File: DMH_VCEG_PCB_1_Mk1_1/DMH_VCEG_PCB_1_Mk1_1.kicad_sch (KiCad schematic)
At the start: 0 parts

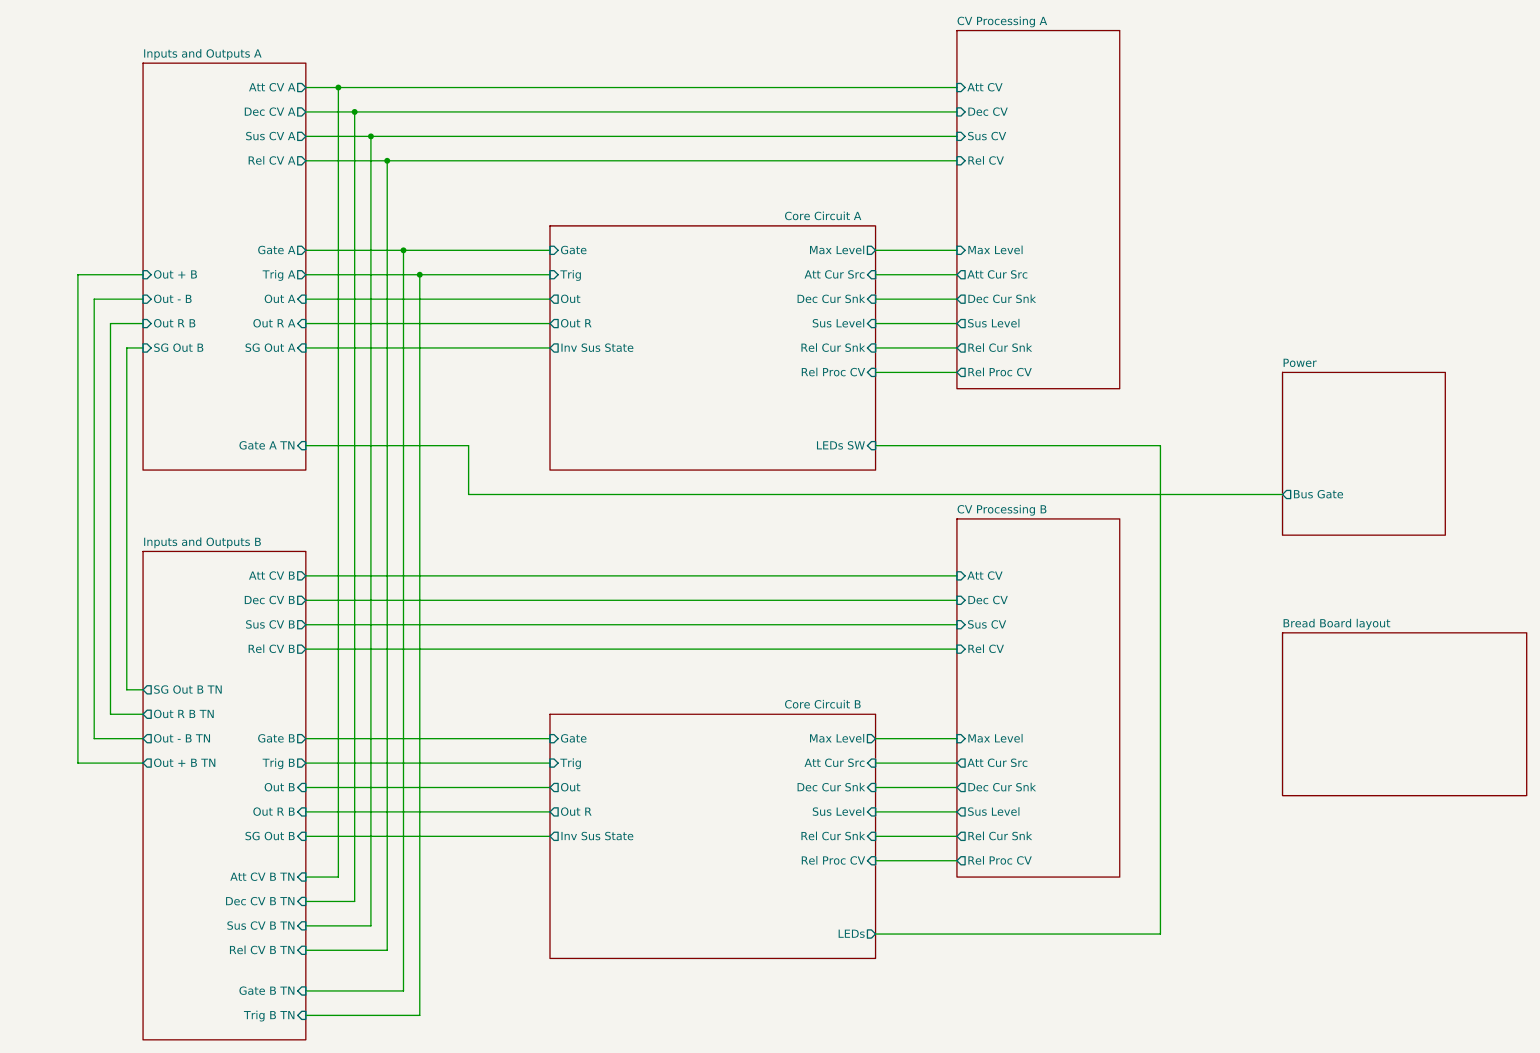
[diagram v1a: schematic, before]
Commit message: Fixed normalled tip routing for CV and Gate
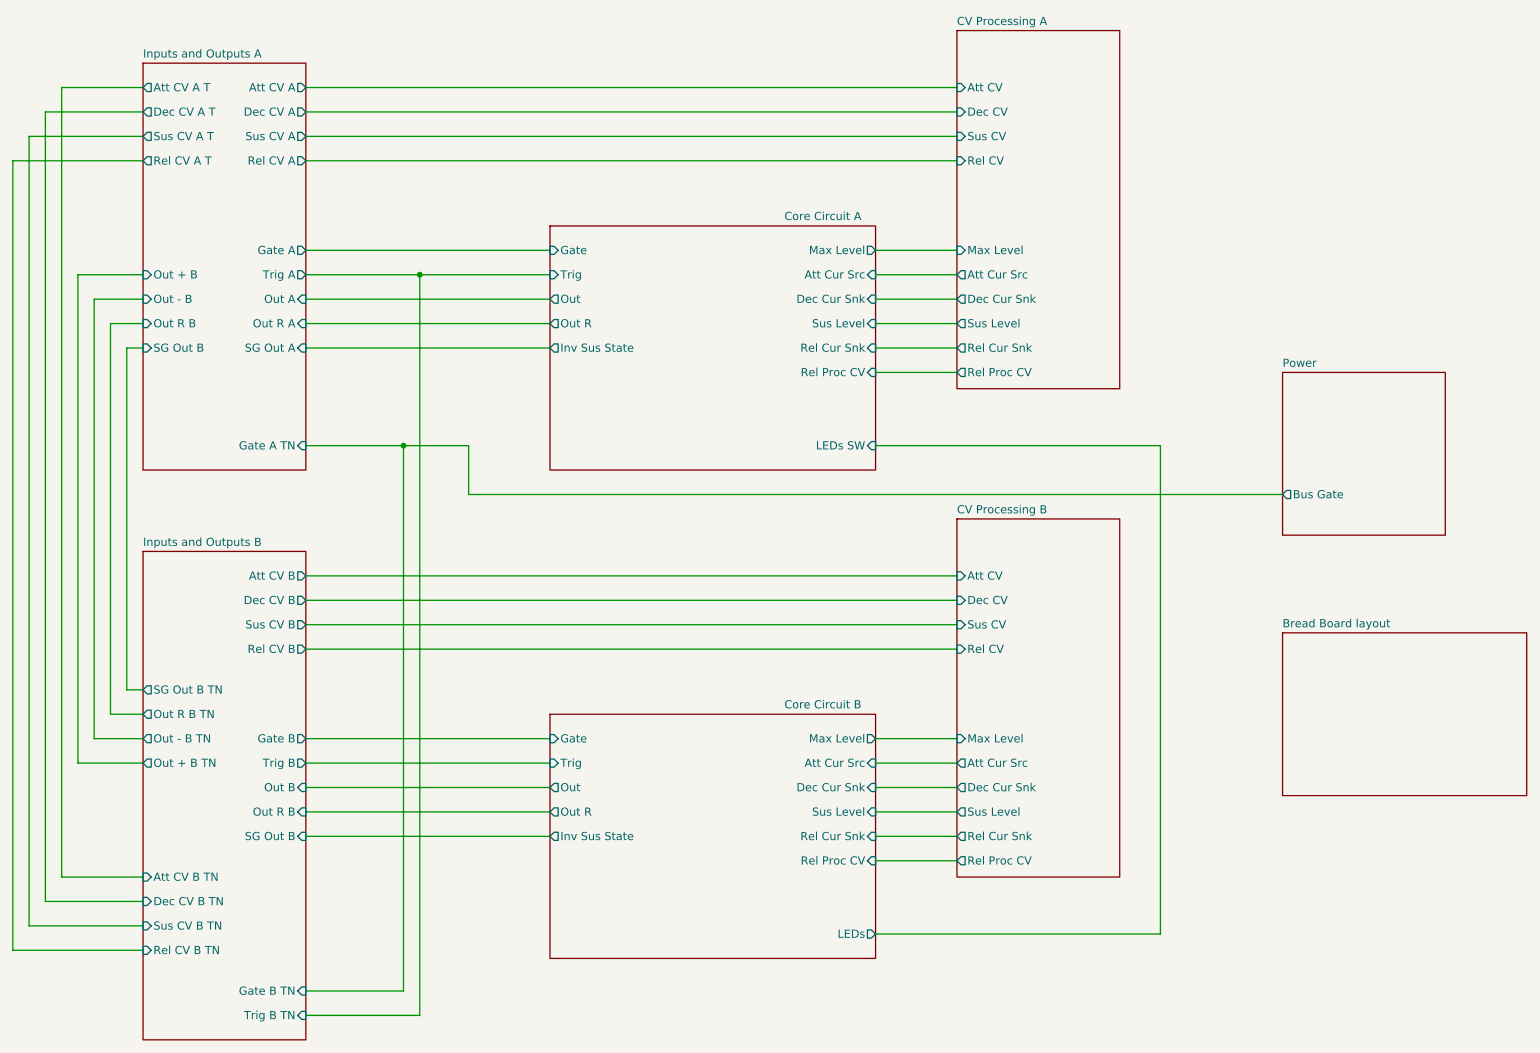
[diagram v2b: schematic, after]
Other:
- sheet Inputs and Outputs A ports: added Att CV A T, Dec CV A T, Rel CV A T, Sus CV A T; removed none
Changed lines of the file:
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@@
 	)
 	(junction
-		(at 78.74 54.61)
+		(at 78.74 85.09)
 		(diameter 0)
 		(color 0 0 0 0)
 	)
-	(junction
-		(at 73.66 36.83)
-		(diameter 0)
-		(color 0 0 0 0)
-	)
-	(junction
-		(at 68.58 29.21)
-		(diameter 0)
-		(color 0 0 0 0)
-	)
-	(junction
-		(at 76.2 40.64)
-		(diameter 0)
-		(color 0 0 0 0)
-	)
-	(junction
-		(at 71.12 33.02)
-		(diameter 0)
-		(color 0 0 0 0)
-	)
-	(wire
-		(pts
-			(xy 63.5 36.83) (xy 73.66 36.83)
+	(wire
+		(pts
+			(xy 63.5 36.83) (xy 165.1 36.83)
 		)
 		(stroke
@@
 	(wire
 		(pts
+			(xy 38.1 40.64) (xy 17.78 40.64)
+		)
+		(stroke
+			(width 0)
+			(type default)
+		)
+	)
+	(wire
+		(pts
 			(xy 152.4 146.05) (xy 165.1 146.05)
 		)
@@
 	(wire
 		(pts
-			(xy 63.5 160.02) (xy 73.66 160.02)
-		)
-		(stroke
-			(width 0)
-			(type default)
-		)
-	)
-	(wire
-		(pts
 			(xy 63.5 173.99) (xy 81.28 173.99)
 		)
@@
 	(wire
 		(pts
-			(xy 76.2 40.64) (xy 165.1 40.64)
+			(xy 78.74 85.09) (xy 88.9 85.09)
 		)
 		(stroke
@@
 	(wire
 		(pts
+			(xy 38.1 33.02) (xy 22.86 33.02)
+		)
+		(stroke
+			(width 0)
+			(type default)
+		)
+	)
+	(wire
+		(pts
 			(xy 63.5 105.41) (xy 165.1 105.41)
 		)
@@
 	(wire
 		(pts
-			(xy 63.5 152.4) (xy 68.58 152.4)
-		)
-		(stroke
-			(width 0)
-			(type default)
-		)
-	)
-	(wire
-		(pts
-			(xy 63.5 85.09) (xy 88.9 85.09)
+			(xy 17.78 40.64) (xy 17.78 163.83)
+		)
+		(stroke
+			(width 0)
+			(type default)
+		)
+	)
+	(wire
+		(pts
+			(xy 22.86 156.21) (xy 38.1 156.21)
+		)
+		(stroke
+			(width 0)
+			(type default)
+		)
+	)
+	(wire
+		(pts
+			(xy 63.5 85.09) (xy 78.74 85.09)
 		)
 		(stroke
@@
 	(wire
 		(pts
-			(xy 73.66 160.02) (xy 73.66 36.83)
+			(xy 38.1 29.21) (xy 25.4 29.21)
+		)
+		(stroke
+			(width 0)
+			(type default)
+		)
+	)
+	(wire
+		(pts
+			(xy 25.4 152.4) (xy 38.1 152.4)
 		)
 		(stroke
@@
 	(wire
 		(pts
-			(xy 63.5 54.61) (xy 78.74 54.61)
+			(xy 63.5 54.61) (xy 101.6 54.61)
+		)
+		(stroke
+			(width 0)
+			(type default)
+		)
+	)
+	(wire
+		(pts
+			(xy 78.74 85.09) (xy 78.74 170.18)
 		)
 		(stroke
@@
 	(wire
 		(pts
-			(xy 68.58 29.21) (xy 165.1 29.21)
+			(xy 63.5 29.21) (xy 165.1 29.21)
+		)
+		(stroke
+			(width 0)
+			(type default)
+		)
+	)
+	(wire
+		(pts
+			(xy 20.32 160.02) (xy 38.1 160.02)
 		)
 		(stroke
@@
 	(wire
 		(pts
-			(xy 76.2 163.83) (xy 76.2 40.64)
-		)
-		(stroke
-			(width 0)
-			(type default)
-		)
-	)
-	(wire
-		(pts
 			(xy 152.4 73.66) (xy 165.1 73.66)
 		)
@@
 	(wire
 		(pts
-			(xy 73.66 36.83) (xy 165.1 36.83)
-		)
-		(stroke
-			(width 0)
-			(type default)
-		)
-	)
-	(wire
-		(pts
-			(xy 63.5 156.21) (xy 71.12 156.21)
-		)
-		(stroke
-			(width 0)
-			(type default)
-		)
-	)
-	(wire
-		(pts
-			(xy 78.74 170.18) (xy 78.74 54.61)
-		)
-		(stroke
-			(width 0)
-			(type default)
-		)
-	)
-	(wire
-		(pts
-			(xy 78.74 54.61) (xy 101.6 54.61)
+			(xy 38.1 36.83) (xy 20.32 36.83)
+		)
+		(stroke
+			(width 0)
+			(type default)
+		)
+	)
+	(wire
+		(pts
+			(xy 22.86 33.02) (xy 22.86 156.21)
 		)
 		(stroke
@@
 	(wire
 		(pts
-			(xy 71.12 156.21) (xy 71.12 33.02)
-		)
-		(stroke
-			(width 0)
-			(type default)
-		)
-	)
-	(wire
-		(pts
 			(xy 196.85 161.29) (xy 196.85 85.09)
 		)
@@
 	(wire
 		(pts
-			(xy 63.5 40.64) (xy 76.2 40.64)
+			(xy 63.5 40.64) (xy 165.1 40.64)
 		)
 		(stroke
@@
 	(wire
 		(pts
-			(xy 63.5 163.83) (xy 76.2 163.83)
-		)
-		(stroke
-			(width 0)
-			(type default)
-		)
-	)
-	(wire
-		(pts
 			(xy 63.5 109.22) (xy 165.1 109.22)
 		)
@@
 	(wire
 		(pts
-			(xy 63.5 29.21) (xy 68.58 29.21)
-		)
-		(stroke
-			(width 0)
-			(type default)
-		)
-	)
-	(wire
-		(pts
 			(xy 152.4 62.23) (xy 165.1 62.23)
 		)
@@
 	(wire
 		(pts
+			(xy 17.78 163.83) (xy 38.1 163.83)
+		)
+		(stroke
+			(width 0)
+			(type default)
+		)
+	)
+	(wire
+		(pts
 			(xy 152.4 161.29) (xy 196.85 161.29)
 		)
@@
 	(wire
 		(pts
-			(xy 68.58 29.21) (xy 68.58 152.4)
-		)
-		(stroke
-			(width 0)
-			(type default)
-		)
-	)
-	(wire
-		(pts
 			(xy 27.94 134.62) (xy 27.94 58.42)
 		)
@@
 	(wire
 		(pts
+			(xy 20.32 36.83) (xy 20.32 160.02)
+		)
+		(stroke
+			(width 0)
+			(type default)
+		)
+	)
+	(wire
+		(pts
 			(xy 152.4 54.61) (xy 165.1 54.61)
 		)
@@
 	(wire
 		(pts
-			(xy 63.5 33.02) (xy 71.12 33.02)
-		)
-		(stroke
-			(width 0)
-			(type default)
-		)
-	)
-	(wire
-		(pts
 			(xy 152.4 142.24) (xy 165.1 142.24)
 		)
@@
 	(wire
 		(pts
-			(xy 71.12 33.02) (xy 165.1 33.02)
+			(xy 63.5 33.02) (xy 165.1 33.02)
+		)
+		(stroke
+			(width 0)
+			(type default)
+		)
+	)
+	(wire
+		(pts
+			(xy 25.4 29.21) (xy 25.4 152.4)
 		)
 		(stroke
@@
 		)
 		(pin "Att CV B TN" input
-			(at 63.5 152.4 0)
-			(effects
-				(font
-					(size 1.27 1.27)
-				)
-				(justify right)
+			(at 38.1 152.4 180)
+			(effects
+				(font
+					(size 1.27 1.27)
+				)
+				(justify left)
 			)
 		)
 		(pin "Dec CV B TN" input
-			(at 63.5 156.21 0)
-			(effects
-				(font
-					(size 1.27 1.27)
-				)
-				(justify right)
+			(at 38.1 156.21 180)
+			(effects
+				(font
+					(size 1.27 1.27)
+				)
+				(justify left)
 			)
 		)
@@
 		)
 		(pin "Rel CV B TN" input
-			(at 63.5 163.83 0)
-			(effects
-				(font
-					(size 1.27 1.27)
-				)
-				(justify right)
+			(at 38.1 163.83 180)
+			(effects
+				(font
+					(size 1.27 1.27)
+				)
+				(justify left)
 			)
 		)
@@
 		)
 		(pin "Sus CV B TN" input
-			(at 63.5 160.02 0)
-			(effects
-				(font
-					(size 1.27 1.27)
-				)
-				(justify right)
+			(at 38.1 160.02 180)
+			(effects
+				(font
+					(size 1.27 1.27)
+				)
+				(justify left)
 			)
 		)
@@
 			)
 		)
+		(pin "Att CV A T" output
+			(at 38.1 29.21 180)
+			(effects
+				(font
+					(size 1.27 1.27)
+				)
+				(justify left)
+			)
+		)
+		(pin "Dec CV A T" output
+			(at 38.1 33.02 180)
+			(effects
+				(font
+					(size 1.27 1.27)
+				)
+				(justify left)
+			)
+		)
+		(pin "Rel CV A T" output
+			(at 38.1 40.64 180)
+			(effects
+				(font
+					(size 1.27 1.27)
+				)
+				(justify left)
+			)
+		)
+		(pin "Sus CV A T" output
+			(at 38.1 36.83 180)
+			(effects
+				(font
+					(size 1.27 1.27)
+				)
+				(justify left)
+			)
+		)
